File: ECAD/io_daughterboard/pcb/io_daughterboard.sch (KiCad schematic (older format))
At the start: 89 parts, among them CON1 BARREL_JACK, J1 XF2L-0625-1A, J2 4-1734839-0, P1 CONN_02X32, P10 CONN_01X06, P11 CONN_01X06, P12 CONN_01X06, P13 CONN_01X06, P14 CONN_01X06, P15 CONN_01X06, P16 CONN_01X06, P17 CONN_01X06, P18 CONN_01X06, P19 CONN_01X04, P2 CONN_02X32, P3 CONN_01X06, P4 CONN_01X06, P5 CONN_01X06, P6 CONN_01X06, P7 CONN_01X06, P8 CONN_01X06, P9 CONN_01X06, SW1 Reset Button, SW2 User Button, U1 FAN5333BSX, U10 SN74LV1T34DCKR, U11 SN74LV1T34DCKR, U2 SPX3819M5-L-3-3, U3 74HC244, U4 74HC244, U5 74HC244, U6 STMPE811QTR, U7 74HC244, U8 74HC244, U9 74HC244

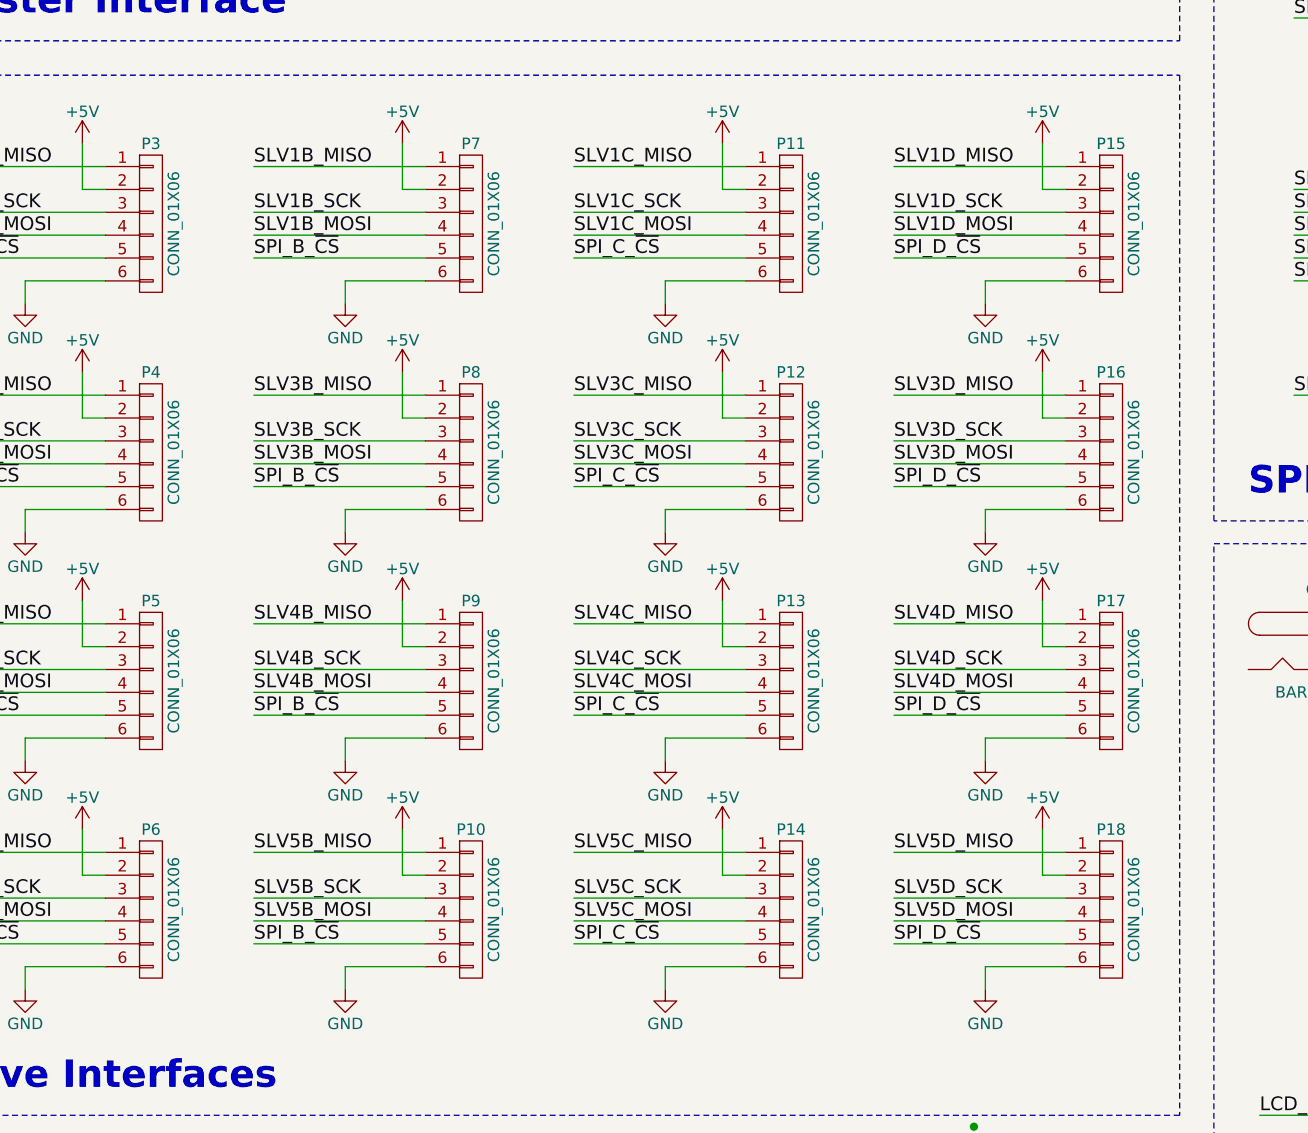
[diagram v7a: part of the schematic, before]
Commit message: Changed values of slave connectors to "Slave 1A" etc.
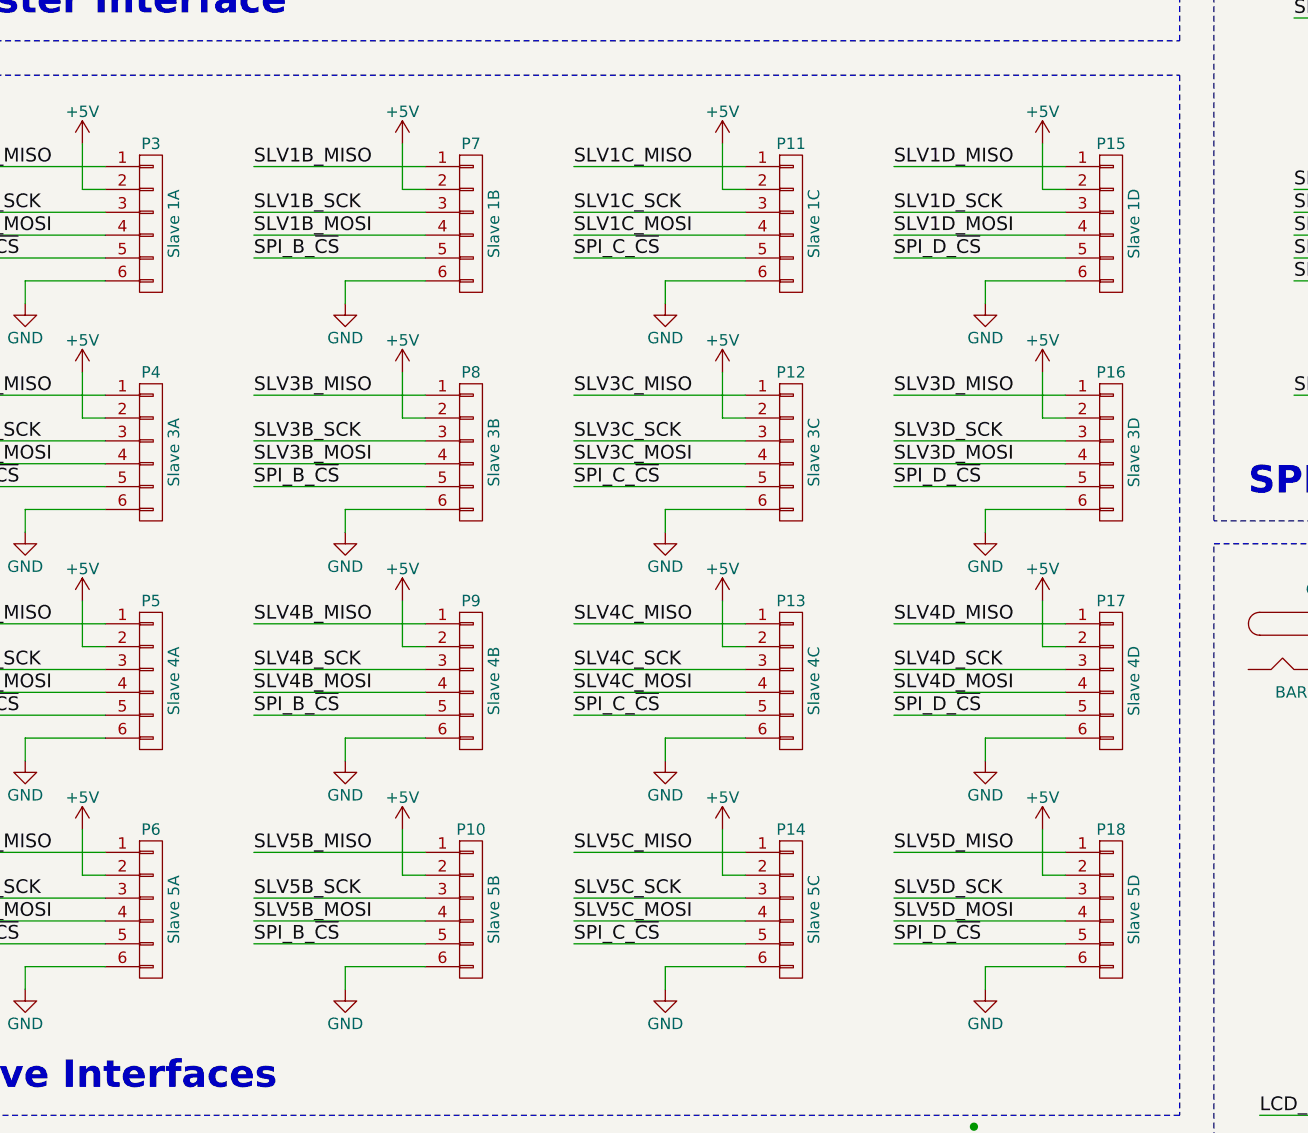
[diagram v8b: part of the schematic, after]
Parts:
- P10: value CONN_01X06 -> Slave 5B
- P11: value CONN_01X06 -> Slave 1C
- P12: value CONN_01X06 -> Slave 3C
- P13: value CONN_01X06 -> Slave 4C
- P14: value CONN_01X06 -> Slave 5C
- P15: value CONN_01X06 -> Slave 1D
- P16: value CONN_01X06 -> Slave 3D
- P17: value CONN_01X06 -> Slave 4D
- P18: value CONN_01X06 -> Slave 5D
- P3: value CONN_01X06 -> Slave 1A
- P4: value CONN_01X06 -> Slave 3A
- P5: value CONN_01X06 -> Slave 4A
- P6: value CONN_01X06 -> Slave 5A
- P7: value CONN_01X06 -> Slave 1B
- P8: value CONN_01X06 -> Slave 3B
- P9: value CONN_01X06 -> Slave 4B
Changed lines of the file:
@@
 P 1750 5500
 F 0 "P3" H 1750 5850 50  0000 C CNN
-F 1 "CONN_01X06" V 1850 5500 50  0000 C CNN
+F 1 "Slave 1A" V 1850 5500 50  0000 C CNN
 F 2 "Pin_Headers:Pin_Header_Straight_2x03_Pitch2.00mm" H 1750 5500 50  0001 C CNN
 F 3 "" H 1750 5500 50  0000 C CNN
@@
 P 3150 5500
 F 0 "P7" H 3150 5850 50  0000 C CNN
-F 1 "CONN_01X06" V 3250 5500 50  0000 C CNN
+F 1 "Slave 1B" V 3250 5500 50  0000 C CNN
 F 2 "Pin_Headers:Pin_Header_Straight_2x03_Pitch2.00mm" H 3150 5500 50  0001 C CNN
 F 3 "" H 3150 5500 50  0000 C CNN
@@
 P 4550 5500
 F 0 "P11" H 4550 5850 50  0000 C CNN
-F 1 "CONN_01X06" V 4650 5500 50  0000 C CNN
+F 1 "Slave 1C" V 4650 5500 50  0000 C CNN
 F 2 "Pin_Headers:Pin_Header_Straight_2x03_Pitch2.00mm" H 4550 5500 50  0001 C CNN
 F 3 "" H 4550 5500 50  0000 C CNN
@@
 P 1750 6500
 F 0 "P4" H 1750 6850 50  0000 C CNN
-F 1 "CONN_01X06" V 1850 6500 50  0000 C CNN
+F 1 "Slave 3A" V 1850 6500 50  0000 C CNN
 F 2 "Pin_Headers:Pin_Header_Straight_2x03_Pitch2.00mm" H 1750 6500 50  0001 C CNN
 F 3 "" H 1750 6500 50  0000 C CNN
@@
 P 3150 6500
 F 0 "P8" H 3150 6850 50  0000 C CNN
-F 1 "CONN_01X06" V 3250 6500 50  0000 C CNN
+F 1 "Slave 3B" V 3250 6500 50  0000 C CNN
 F 2 "Pin_Headers:Pin_Header_Straight_2x03_Pitch2.00mm" H 3150 6500 50  0001 C CNN
 F 3 "" H 3150 6500 50  0000 C CNN
@@
 P 4550 6500
 F 0 "P12" H 4550 6850 50  0000 C CNN
-F 1 "CONN_01X06" V 4650 6500 50  0000 C CNN
+F 1 "Slave 3C" V 4650 6500 50  0000 C CNN
 F 2 "Pin_Headers:Pin_Header_Straight_2x03_Pitch2.00mm" H 4550 6500 50  0001 C CNN
 F 3 "" H 4550 6500 50  0000 C CNN
@@
 P 5950 5500
 F 0 "P15" H 5950 5850 50  0000 C CNN
-F 1 "CONN_01X06" V 6050 5500 50  0000 C CNN
+F 1 "Slave 1D" V 6050 5500 50  0000 C CNN
 F 2 "Pin_Headers:Pin_Header_Straight_2x03_Pitch2.00mm" H 5950 5500 50  0001 C CNN
 F 3 "" H 5950 5500 50  0000 C CNN
@@
 P 5950 6500
 F 0 "P16" H 5950 6850 50  0000 C CNN
-F 1 "CONN_01X06" V 6050 6500 50  0000 C CNN
+F 1 "Slave 3D" V 6050 6500 50  0000 C CNN
 F 2 "Pin_Headers:Pin_Header_Straight_2x03_Pitch2.00mm" H 5950 6500 50  0001 C CNN
 F 3 "" H 5950 6500 50  0000 C CNN
@@
 P 1750 7500
 F 0 "P5" H 1750 7850 50  0000 C CNN
-F 1 "CONN_01X06" V 1850 7500 50  0000 C CNN
+F 1 "Slave 4A" V 1850 7500 50  0000 C CNN
 F 2 "Pin_Headers:Pin_Header_Straight_2x03_Pitch2.00mm" H 1750 7500 50  0001 C CNN
 F 3 "" H 1750 7500 50  0000 C CNN
@@
 P 3150 7500
 F 0 "P9" H 3150 7850 50  0000 C CNN
-F 1 "CONN_01X06" V 3250 7500 50  0000 C CNN
+F 1 "Slave 4B" V 3250 7500 50  0000 C CNN
 F 2 "Pin_Headers:Pin_Header_Straight_2x03_Pitch2.00mm" H 3150 7500 50  0001 C CNN
 F 3 "" H 3150 7500 50  0000 C CNN
@@
 P 4550 7500
 F 0 "P13" H 4550 7850 50  0000 C CNN
-F 1 "CONN_01X06" V 4650 7500 50  0000 C CNN
+F 1 "Slave 4C" V 4650 7500 50  0000 C CNN
 F 2 "Pin_Headers:Pin_Header_Straight_2x03_Pitch2.00mm" H 4550 7500 50  0001 C CNN
 F 3 "" H 4550 7500 50  0000 C CNN
@@
 P 1750 8500
 F 0 "P6" H 1750 8850 50  0000 C CNN
-F 1 "CONN_01X06" V 1850 8500 50  0000 C CNN
+F 1 "Slave 5A" V 1850 8500 50  0000 C CNN
 F 2 "Pin_Headers:Pin_Header_Straight_2x03_Pitch2.00mm" H 1750 8500 50  0001 C CNN
 F 3 "" H 1750 8500 50  0000 C CNN
@@
 P 3150 8500
 F 0 "P10" H 3150 8850 50  0000 C CNN
-F 1 "CONN_01X06" V 3250 8500 50  0000 C CNN
+F 1 "Slave 5B" V 3250 8500 50  0000 C CNN
 F 2 "Pin_Headers:Pin_Header_Straight_2x03_Pitch2.00mm" H 3150 8500 50  0001 C CNN
 F 3 "" H 3150 8500 50  0000 C CNN
@@
 P 4550 8500
 F 0 "P14" H 4550 8850 50  0000 C CNN
-F 1 "CONN_01X06" V 4650 8500 50  0000 C CNN
+F 1 "Slave 5C" V 4650 8500 50  0000 C CNN
 F 2 "Pin_Headers:Pin_Header_Straight_2x03_Pitch2.00mm" H 4550 8500 50  0001 C CNN
 F 3 "" H 4550 8500 50  0000 C CNN
@@
 P 5950 7500
 F 0 "P17" H 5950 7850 50  0000 C CNN
-F 1 "CONN_01X06" V 6050 7500 50  0000 C CNN
+F 1 "Slave 4D" V 6050 7500 50  0000 C CNN
 F 2 "Pin_Headers:Pin_Header_Straight_2x03_Pitch2.00mm" H 5950 7500 50  0001 C CNN
 F 3 "" H 5950 7500 50  0000 C CNN
@@
 P 5950 8500
 F 0 "P18" H 5950 8850 50  0000 C CNN
-F 1 "CONN_01X06" V 6050 8500 50  0000 C CNN
+F 1 "Slave 5D" V 6050 8500 50  0000 C CNN
 F 2 "Pin_Headers:Pin_Header_Straight_2x03_Pitch2.00mm" H 5950 8500 50  0001 C CNN
 F 3 "" H 5950 8500 50  0000 C CNN
